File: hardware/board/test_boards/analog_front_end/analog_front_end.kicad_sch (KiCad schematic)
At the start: 13 parts, among them J1 Conn_01x20_Female, J2 Conn_01x20_Female, U6 LM27762

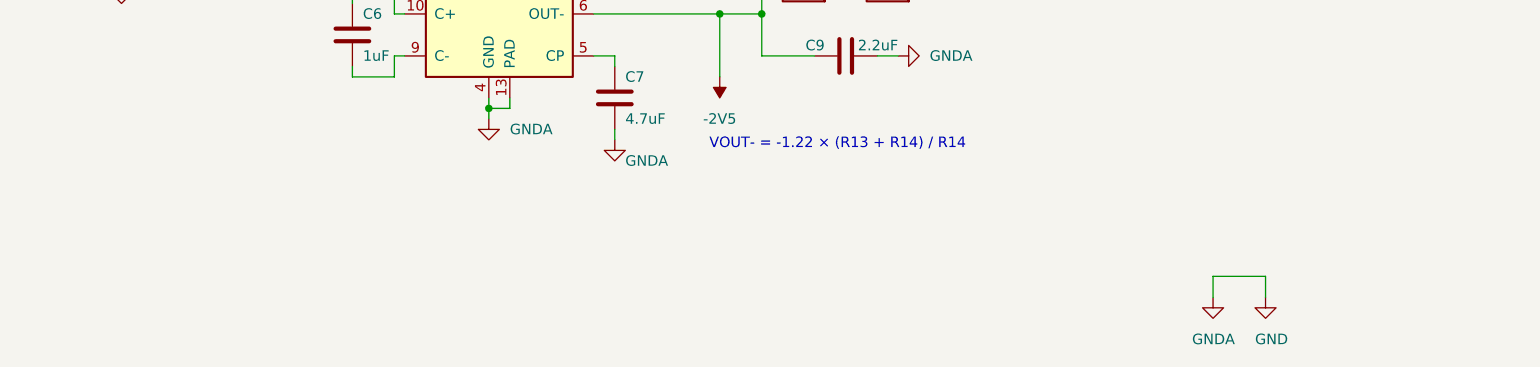
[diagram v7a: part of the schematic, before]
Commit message: add notes to pcb schematic for cleaner power supply layout to reduce spikes
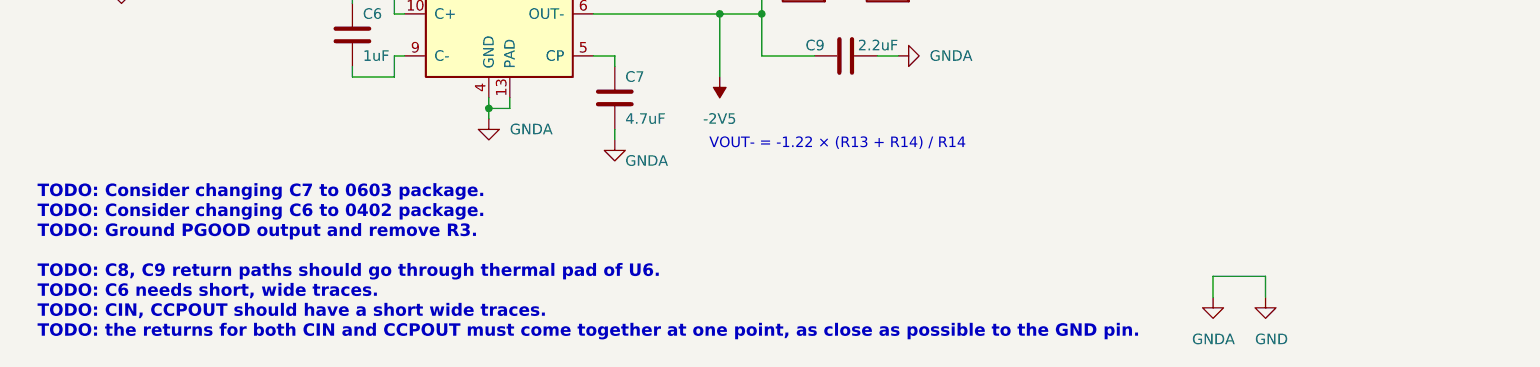
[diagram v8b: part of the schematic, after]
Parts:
- C5: Link https://www.digikey.com/en/products/detail/samsung-electro-mechanics/CL31A226KAHNNNE/3888705 -> https://www.digikey.com/en/products/detail/samsung-electro-mechanics/CL21A226KPCLRNC/5961270; Manufacturer (none) -> Samsung Electro-Mechanics; Manufacturer Number CL31A226KAHNNNE -> CL21A226KPCLRNC; Rated Voltage 25V -> 10V
- U6: Manufacturer (none) -> Texas Instruments; Manufacturer Number (none) -> LM27762DSST
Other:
- note added: "TODO: Consider changing C7 to 0603 package. TODO: Consider changing C6 to 0402 package. TODO: Ground PGOOD output and remove R3. TODO: C8, C9 return paths should go through thermal pad of U6. TODO: C6 needs short, wide traces. TODO: CIN, CCPOUT should have a short wide traces. TODO: the returns for both CIN and CCPOUT must come together at one point, as close as possible to the GND pin."
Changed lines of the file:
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@@
     (effects (font (size 1.27 1.27)) (justify left bottom))
+  )
+  (text "TODO: Consider changing C7 to 0603 package.\nTODO: Consider changing C6 to 0402 package.\nTODO: Ground PGOOD output and remove R3.\n\nTODO: C8, C9 return paths should go through thermal pad of U6.\nTODO: C6 needs short, wide traces.\nTODO: CIN, CCPOUT should have a short wide traces.\nTODO: the returns for both CIN and CCPOUT must come together at one point, as close as possible to the GND pin."
+    (at 15.24 193.04 0)
+    (effects (font (size 1.5 1.5) (thickness 0.4) bold) (justify left bottom))
   )
   (text "GP3" (at 36.83 41.91 0)
@@
     )
     (property "Link" "https://www.digikey.com/en/products/detail/texas-instruments/LM27762DSST/6234952" (id 4) (at 69.85 143.51 0)
+      (effects (font (size 1.27 1.27)) hide)
+    )
+    (property "Manufacturer" "Texas Instruments" (id 5) (at 69.85 143.51 0)
+      (effects (font (size 1.27 1.27)) hide)
+    )
+    (property "Manufacturer Number" "LM27762DSST" (id 6) (at 69.85 143.51 0)
       (effects (font (size 1.27 1.27)) hide)
     )
@@
       (effects (font (size 1.27 1.27)) hide)
     )
-    (property "Datasheet" "https://media.digikey.com/pdf/Data%20Sheets/Samsung%20PDFs/CL31A226KAHNNNE_Spec.pdf" (id 3) (at 25.4 144.78 0)
-      (effects (font (size 1.27 1.27)) hide)
-    )
-    (property "Link" "https://www.digikey.com/en/products/detail/samsung-electro-mechanics/CL31A226KAHNNNE/3888705" (id 4) (at 25.4 144.78 0)
-      (effects (font (size 1.27 1.27)) hide)
-    )
-    (property "Manufacturer Number" "CL31A226KAHNNNE" (id 5) (at 25.4 144.78 0)
+    (property "Datasheet" "https://media.digikey.com/pdf/Data%20Sheets/Samsung%20PDFs/CL21A226KPCLRNC_Spec.pdf" (id 3) (at 25.4 144.78 0)
+      (effects (font (size 1.27 1.27)) hide)
+    )
+    (property "Link" "https://www.digikey.com/en/products/detail/samsung-electro-mechanics/CL21A226KPCLRNC/5961270" (id 4) (at 25.4 144.78 0)
+      (effects (font (size 1.27 1.27)) hide)
+    )
+    (property "Manufacturer Number" "CL21A226KPCLRNC" (id 5) (at 25.4 144.78 0)
       (effects (font (size 1.27 1.27)) hide)
     )
@@
       (effects (font (size 1.27 1.27)) hide)
     )
-    (property "Rated Voltage" "25V" (id 7) (at 25.4 144.78 0)
+    (property "Rated Voltage" "10V" (id 7) (at 25.4 144.78 0)
       (effects (font (size 1.27 1.27)) hide)
     )
@@
       (effects (font (size 1.27 1.27)) hide)
     )
+    (property "Manufacturer" "Samsung Electro-Mechanics" (id 9) (at 25.4 144.78 0)
+      (effects (font (size 1.27 1.27)) hide)
+    )
     (pin "1")
     (pin "2")
@@
       (effects (font (size 1.27 1.27)) hide)
     )
-    (property "Datasheet" "" (id 3) (at 113.03 158.75 0)
+    (property "Datasheet" "https://search.murata.co.jp/Ceramy/image/img/A01X/G101/ENG/GRM188C71E225KE11-01.pdf" (id 3) (at 113.03 158.75 0)
       (effects (font (size 1.27 1.27)) hide)
     )
@@
       (effects (font (size 1.27 1.27)) hide)
     )
-    (property "Datasheet" "~" (id 3) (at 85.09 163.83 0)
+    (property "Datasheet" "https://search.murata.co.jp/Ceramy/image/img/A01X/G101/ENG/GRM21BZ71H475KE15-01.pdf" (id 3) (at 85.09 163.83 0)
       (effects (font (size 1.27 1.27)) hide)
     )
@@
       (effects (font (size 1.27 1.27)) hide)
     )
-    (property "Datasheet" "" (id 3) (at 113.03 133.35 0)
+    (property "Datasheet" "https://search.murata.co.jp/Ceramy/image/img/A01X/G101/ENG/GRM188C71E225KE11-01.pdf" (id 3) (at 113.03 133.35 0)
       (effects (font (size 1.27 1.27)) hide)
     )
@@
     )
     (path "/8ca25f6d-cadc-4d60-beba-2de6b7c14b93/902054eb-0b76-4847-b65b-9e2279644495"
-      (reference "R42") (unit 1) (value "390") (footprint "Resistor_SMD:R_0402_1005Metric_Pad0.72x0.64mm_HandSolder")
+      (reference "R42") (unit 1) (value "100") (footprint "Resistor_SMD:R_0402_1005Metric_Pad0.72x0.64mm_HandSolder")
     )
     (path "/8ca25f6d-cadc-4d60-beba-2de6b7c14b93/0341274f-310c-4dc7-b5fc-46da927889c7"
-      (reference "R43") (unit 1) (value "390") (footprint "Resistor_SMD:R_0402_1005Metric_Pad0.72x0.64mm_HandSolder")
+      (reference "R43") (unit 1) (value "2K") (footprint "Resistor_SMD:R_0402_1005Metric_Pad0.72x0.64mm_HandSolder")
     )
     (path "/8ca25f6d-cadc-4d60-beba-2de6b7c14b93/174fe534-9610-415a-b69e-56ad988bb1d1"
